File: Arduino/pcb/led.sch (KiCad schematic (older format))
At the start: 12 parts, among them Q1 IRLML2060, Q2 IRLML2060, Q3 IRLML2060, U4 74HC595

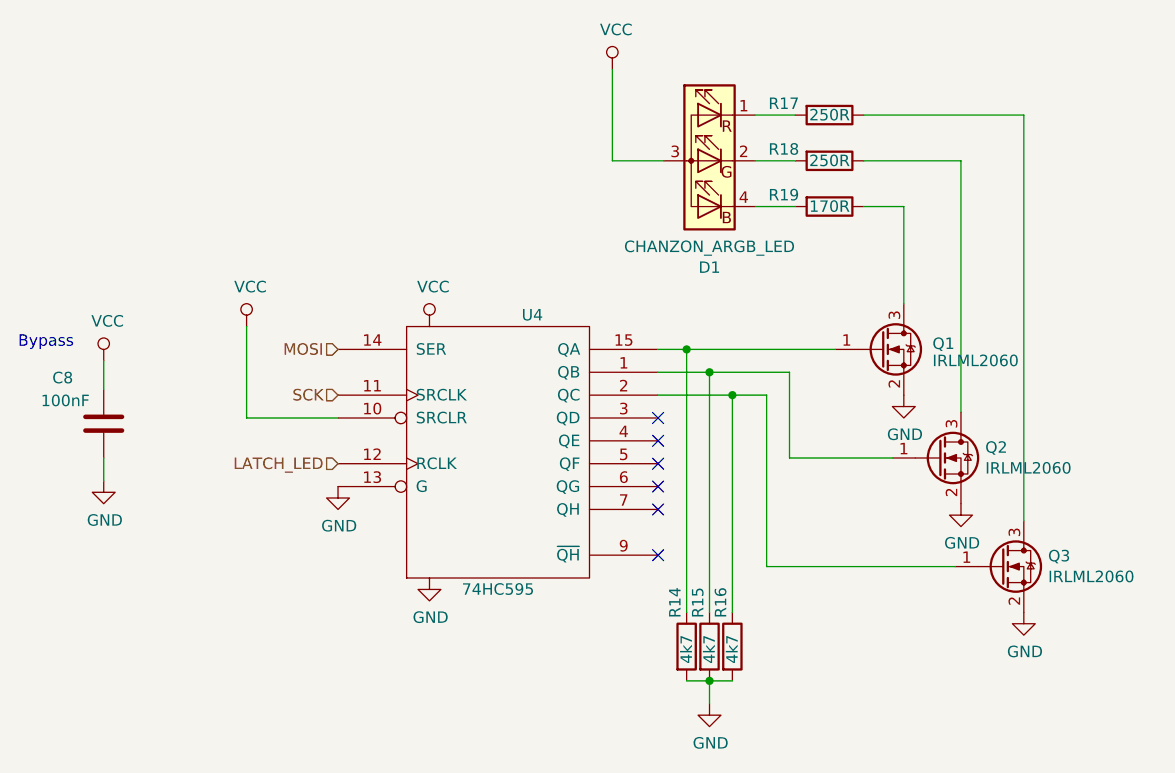
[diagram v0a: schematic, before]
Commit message: pcb: swap red and blue pin on RGB led
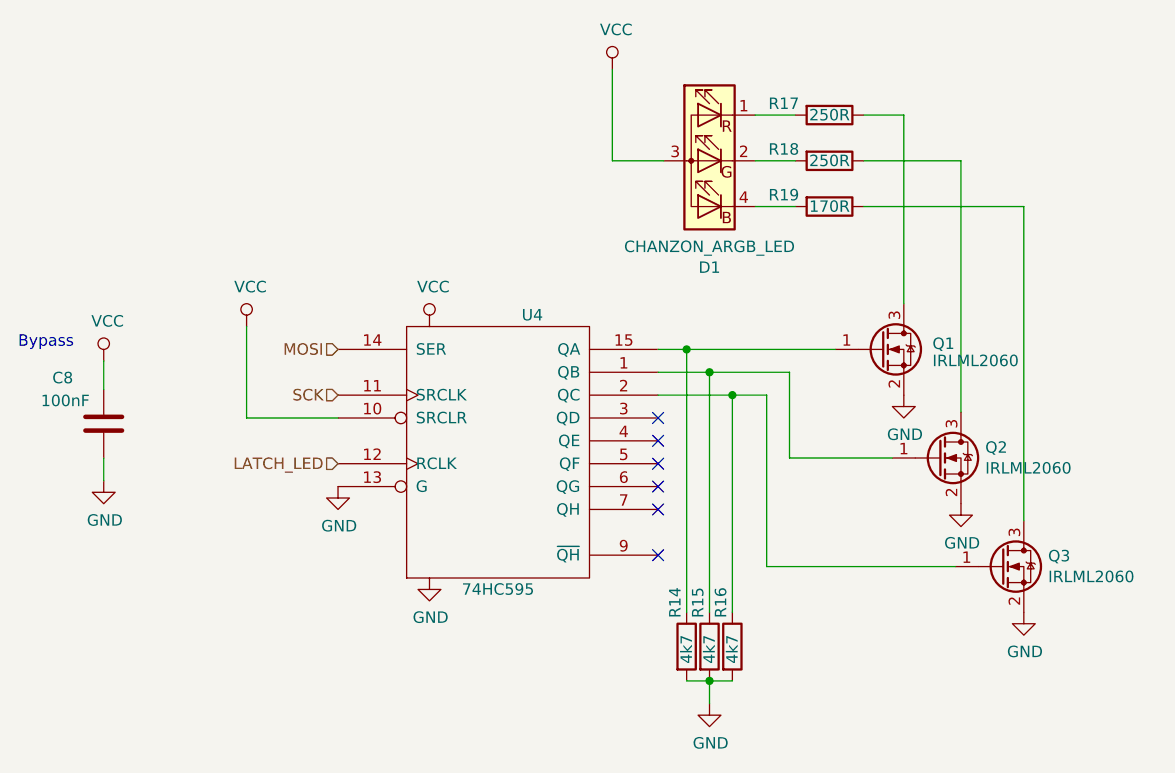
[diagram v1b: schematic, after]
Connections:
- net at R17.1: now also Q1.3 (D); no longer Q3.3 (D)
- net at R19.1: now also Q3.3 (D); no longer Q1.3 (D)
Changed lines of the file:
@@
 EESchema Schematic File Version 4
 LIBS:floppyorgel-cache
-EELAYER 29 0
+EELAYER 30 0
 EELAYER END
 $Descr A4 11693 8268
@@
 	7500 3225 7500 2125
 Wire Wire Line
-	7775 1925 7775 3700
-Wire Wire Line
 	6175 2950 6300 2950
 $Comp
@@
 	1    0    0    -1
 $EndComp
-Connection ~ 6300 2950
 $Comp
 L power:GND #PWR042
@@
 	6750 3425 7200 3425
 Wire Wire Line
-	6300 2950 6950 2950
-Wire Wire Line
-	7250 2750 7250 2325
-Wire Wire Line
 	5975 2125 6200 2125
 Wire Wire Line
 	6600 1925 6775 1925
 Wire Wire Line
-	7075 1925 7775 1925
-Wire Wire Line
 	7075 2125 7500 2125
 Wire Wire Line
-	7075 2325 7250 2325
-Wire Wire Line
 	6600 2125 6775 2125
 Wire Wire Line
@@
 EndData
 $EndBitmap
+Connection ~ 6300 2950
+Wire Wire Line
+	6300 2950 6950 2950
+Wire Wire Line
+	7075 2325 7775 2325
+Wire Wire Line
+	7775 2325 7775 3700
+Wire Wire Line
+	7075 1925 7250 1925
+Wire Wire Line
+	7250 1925 7250 2750
 $EndSCHEMATC

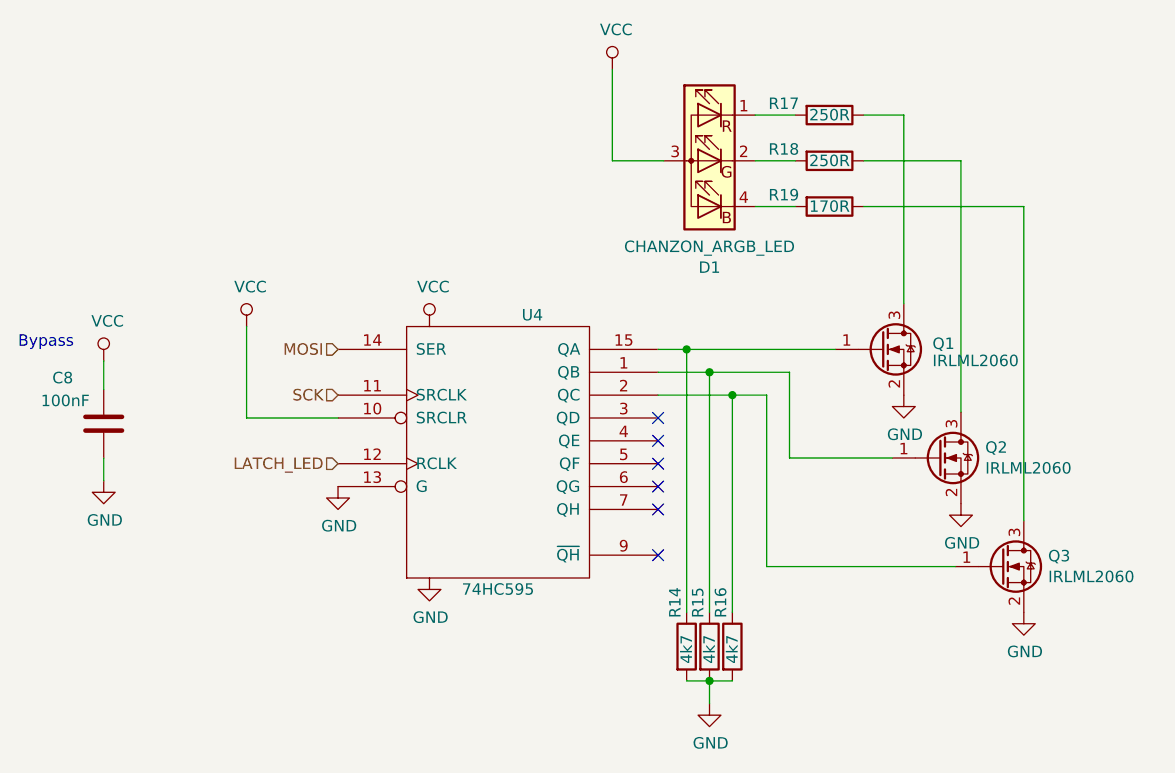
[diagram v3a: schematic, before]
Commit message: pcb / led: remove hc595 shift register / connect led directly
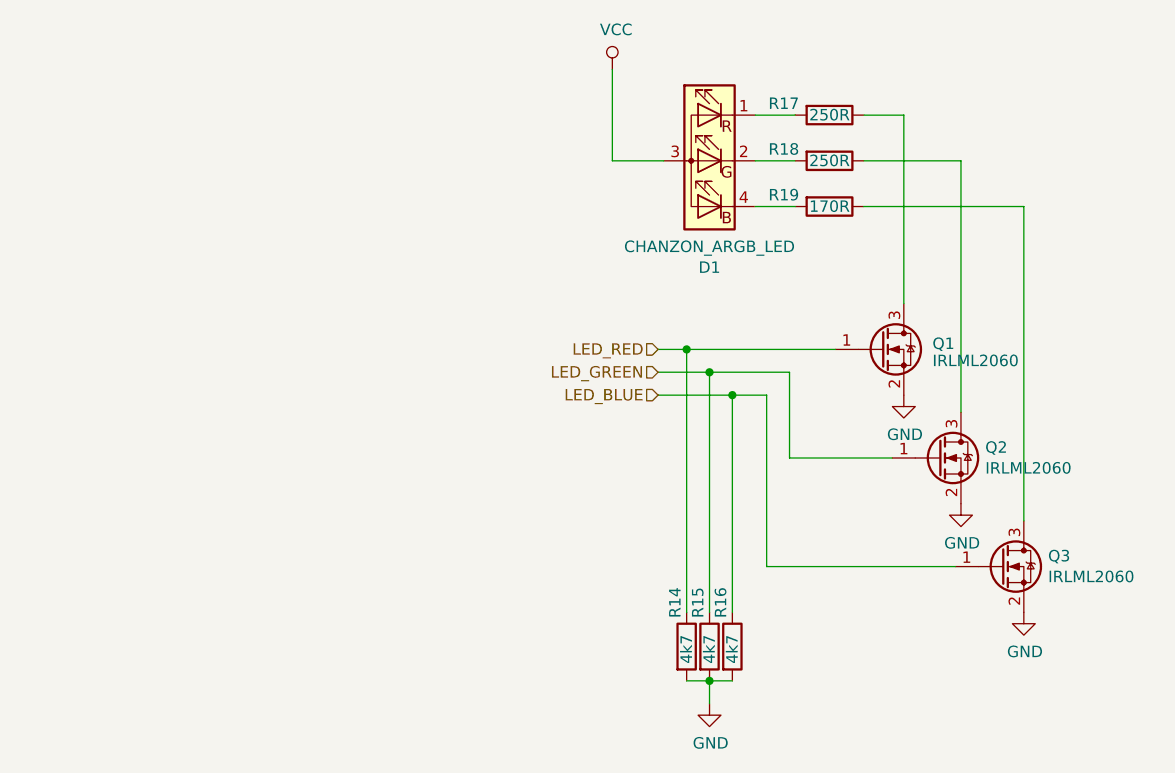
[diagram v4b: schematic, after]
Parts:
- removed C8: 100nF, Capacitor_SMD:C_0805_2012Metric, symbol Device:C
- removed U4: 74HC595, Package_SO:TSSOP-16_4.4x5mm_P0.65mm, symbol floppyorgel-rescue:74HC595-74xx
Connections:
- net LED_RED: now reaches Q1.1 (G), R14.1
- net LED_GREEN: now reaches Q2.1 (G), R15.1
- net LED_BLUE: now reaches Q3.1 (G), R16.1
- no-connect marks 6 -> 0
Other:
- note removed: "Bypass"
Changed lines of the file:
@@
 $EndDescr
 $Comp
-L power:VCC #PWR039
-U 1 1 5D09B29E
-P 5175 2850
-F 0 "#PWR039" H 5175 2700 50  0001 C CNN
-F 1 "VCC" H 5192 3023 50  0000 C CNN
-F 2 "" H 5175 2850 50  0001 C CNN
-F 3 "" H 5175 2850 50  0001 C CNN
-	1    5175 2850
-	1    0    0    -1
-$EndComp
-$Comp
-L power:GND #PWR040
-U 1 1 5D09B2A4
-P 5175 3950
-F 0 "#PWR040" H 5175 3700 50  0001 C CNN
-F 1 "GND" H 5180 3777 50  0000 C CNN
-F 2 "" H 5175 3950 50  0001 C CNN
-F 3 "" H 5175 3950 50  0001 C CNN
-	1    5175 3950
-	1    0    0    -1
-$EndComp
-$Comp
-L power:GND #PWR038
-U 1 1 5D09B2C0
-P 4775 3550
-F 0 "#PWR038" H 4775 3300 50  0001 C CNN
-F 1 "GND" H 4780 3377 50  0000 C CNN
-F 2 "" H 4775 3550 50  0001 C CNN
-F 3 "" H 4775 3550 50  0001 C CNN
-	1    4775 3550
-	1    0    0    -1
-$EndComp
-Wire Wire Line
-	4775 3250 4375 3250
-$Comp
-L power:VCC #PWR037
-U 1 1 5D09B2C7
-P 4375 2850
-F 0 "#PWR037" H 4375 2700 50  0001 C CNN
-F 1 "VCC" H 4392 3023 50  0000 C CNN
-F 2 "" H 4375 2850 50  0001 C CNN
-F 3 "" H 4375 2850 50  0001 C CNN
-	1    4375 2850
-	1    0    0    -1
-$EndComp
-NoConn ~ 6175 3250
-NoConn ~ 6175 3350
-NoConn ~ 6175 3450
-NoConn ~ 6175 3550
-NoConn ~ 6175 3650
-NoConn ~ 6175 3850
-$Comp
-L floppyorgel-rescue:74HC595-74xx U4
-U 1 1 5D09B2D3
-P 5475 3400
-F 0 "U4" H 5625 4000 50  0000 C CNN
-F 1 "74HC595" H 5475 2800 50  0000 C CNN
-F 2 "Package_SO:TSSOP-16_4.4x5mm_P0.65mm" H 5475 3400 50  0001 C CNN
-F 3 "" H 5475 3400 50  0001 C CNN
-	1    5475 3400
-	1    0    0    -1
-$EndComp
-Wire Wire Line
-	4375 2850 4375 3250
-Text HLabel 4775 2950 0    50   Input ~ 0
-MOSI
-Text HLabel 4775 3150 0    50   Input ~ 0
-SCK
-Text HLabel 4775 3450 0    50   Input ~ 0
-LATCH_LED
-$Comp
-L Device:C C?
-U 1 1 5D18829B
-P 3750 3275
-AR Path="/5D18829B" Ref="C?"  Part="1"
-AR Path="/5CCFEC3E/5D18829B" Ref="C?"  Part="1"
-AR Path="/5CD3FBA6/5D18829B" Ref="C8"  Part="1"
-F 0 "C8" H 3525 3475 50  0000 L CNN
-F 1 "100nF" H 3475 3375 50  0000 L CNN
-F 2 "Capacitor_SMD:C_0805_2012Metric" H 3788 3125 50  0001 C CNN
-F 3 "~" H 3750 3275 50  0001 C CNN
-	1    3750 3275
-	1    0    0    -1
-$EndComp
-$Comp
-L power:VCC #PWR?
-U 1 1 5D1882A1
-P 3750 3000
-AR Path="/5CCFEC3E/5D1882A1" Ref="#PWR?"  Part="1"
-AR Path="/5CD3FBA6/5D1882A1" Ref="#PWR035"  Part="1"
-F 0 "#PWR035" H 3750 2850 50  0001 C CNN
-F 1 "VCC" H 3767 3173 50  0000 C CNN
-F 2 "" H 3750 3000 50  0001 C CNN
-F 3 "" H 3750 3000 50  0001 C CNN
-	1    3750 3000
-	1    0    0    -1
-$EndComp
-$Comp
-L power:GND #PWR?
-U 1 1 5D1882A7
-P 3750 3525
-AR Path="/5CCFEC3E/5D1882A7" Ref="#PWR?"  Part="1"
-AR Path="/5CD3FBA6/5D1882A7" Ref="#PWR036"  Part="1"
-F 0 "#PWR036" H 3750 3275 50  0001 C CNN
-F 1 "GND" H 3755 3352 50  0000 C CNN
-F 2 "" H 3750 3525 50  0001 C CNN
-F 3 "" H 3750 3525 50  0001 C CNN
-	1    3750 3525
-	1    0    0    -1
-$EndComp
-Wire Wire Line
-	3750 3000 3750 3125
-Wire Wire Line
-	3750 3425 3750 3525
-Text Notes 3375 2950 0    50   ~ 0
-Bypass
-$Comp
 L Device:R R18
 U 1 1 5CDFA92E
@@
 Wire Wire Line
 	7250 1925 7250 2750
+Text HLabel 6175 2950 0    50   Input ~ 0
+LED_RED
+Text HLabel 6175 3050 0    50   Input ~ 0
+LED_GREEN
+Text HLabel 6175 3150 0    50   Input ~ 0
+LED_BLUE
 $EndSCHEMATC

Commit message: pcb: reannotate symbols
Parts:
- renumbered R14 to R1, R15 to R2, R16 to R3, R17 to R4, R18 to R5, R19 to R6
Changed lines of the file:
@@
 $EndDescr
 $Comp
-L Device:R R18
+L Device:R R5
 U 1 1 5CDFA92E
 P 6925 2125
-F 0 "R18" V 6875 1925 50  0000 C CNN
+F 0 "R5" V 6875 1925 50  0000 C CNN
 F 1 "250R" V 6925 2125 50  0000 C CNN
 F 2 "Resistor_SMD:R_0805_2012Metric" V 6855 2125 50  0001 C CNN
@@
 $EndComp
 $Comp
-L Device:R R17
+L Device:R R4
 U 1 1 5CDFACA1
 P 6925 1925
-F 0 "R17" V 6875 1725 50  0000 C CNN
+F 0 "R4" V 6875 1725 50  0000 C CNN
 F 1 "250R" V 6925 1925 50  0000 C CNN
 F 2 "Resistor_SMD:R_0805_2012Metric" V 6855 1925 50  0001 C CNN
@@
 $EndComp
 $Comp
-L power:GND #PWR043
+L power:GND #PWR06
 U 1 1 5CE5B10B
 P 7250 3150
-F 0 "#PWR043" H 7250 2900 50  0001 C CNN
+F 0 "#PWR06" H 7250 2900 50  0001 C CNN
 F 1 "GND" H 7255 2977 50  0000 C CNN
 F 2 "" H 7250 3150 50  0001 C CNN
@@
 $EndComp
 $Comp
-L Device:R R19
+L Device:R R6
 U 1 1 5CDFAF66
 P 6925 2325
-F 0 "R19" V 6875 2125 50  0000 C CNN
+F 0 "R6" V 6875 2125 50  0000 C CNN
 F 1 "170R" V 6925 2325 50  0000 C CNN
 F 2 "Resistor_SMD:R_0805_2012Metric" V 6855 2325 50  0001 C CNN
@@
 $EndComp
 $Comp
-L power:VCC #PWR041
+L power:VCC #PWR04
 U 1 1 5CEB296C
 P 5975 1725
-F 0 "#PWR041" H 5975 1575 50  0001 C CNN
+F 0 "#PWR04" H 5975 1575 50  0001 C CNN
 F 1 "VCC" H 5992 1898 50  0000 C CNN
 F 2 "" H 5975 1725 50  0001 C CNN
@@
 $EndComp
 $Comp
-L power:GND #PWR044
+L power:GND #PWR07
 U 1 1 5CF166DE
 P 7500 3625
-F 0 "#PWR044" H 7500 3375 50  0001 C CNN
+F 0 "#PWR07" H 7500 3375 50  0001 C CNN
 F 1 "GND" H 7505 3452 50  0000 C CNN
 F 2 "" H 7500 3625 50  0001 C CNN
@@
 $EndComp
 $Comp
-L power:GND #PWR045
+L power:GND #PWR08
 U 1 1 5CF1E097
 P 7775 4100
-F 0 "#PWR045" H 7775 3850 50  0001 C CNN
+F 0 "#PWR08" H 7775 3850 50  0001 C CNN
 F 1 "GND" H 7780 3927 50  0000 C CNN
 F 2 "" H 7775 4100 50  0001 C CNN
@@
 	6175 2950 6300 2950
 $Comp
-L Device:R R14
+L Device:R R1
 U 1 1 5CF4F3BC
 P 6300 4250
-F 0 "R14" V 6250 4375 50  0000 L CNN
+F 0 "R1" V 6250 4375 50  0000 L CNN
 F 1 "4k7" V 6300 4175 50  0000 L CNN
 F 2 "Resistor_SMD:R_0805_2012Metric" V 6230 4250 50  0001 C CNN
@@
 $EndComp
 $Comp
-L Device:R R15
+L Device:R R2
 U 1 1 5CF563D6
 P 6400 4250
-F 0 "R15" V 6350 4375 50  0000 L CNN
+F 0 "R2" V 6350 4375 50  0000 L CNN
 F 1 "4k7" V 6400 4175 50  0000 L CNN
 F 2 "Resistor_SMD:R_0805_2012Metric" V 6330 4250 50  0001 C CNN
@@
 $EndComp
 $Comp
-L Device:R R16
+L Device:R R3
 U 1 1 5CF56A72
 P 6500 4250
-F 0 "R16" V 6450 4375 50  0000 L CNN
+F 0 "R3" V 6450 4375 50  0000 L CNN
 F 1 "4k7" V 6500 4175 50  0000 L CNN
 F 2 "Resistor_SMD:R_0805_2012Metric" V 6430 4250 50  0001 C CNN
@@
 $EndComp
 $Comp
-L power:GND #PWR042
+L power:GND #PWR05
 U 1 1 5CF83BE3
 P 6400 4500
-F 0 "#PWR042" H 6400 4250 50  0001 C CNN
+F 0 "#PWR05" H 6400 4250 50  0001 C CNN
 F 1 "GND" H 6405 4327 50  0000 C CNN
 F 2 "" H 6400 4500 50  0001 C CNN
